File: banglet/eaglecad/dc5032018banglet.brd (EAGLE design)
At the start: 39.8 x 22.6 mm, 43 parts, among them Q3 DMG3415U-7, U2 AP2112(3.3V), U3 MCP73831T-2ACI/OT, U4 CP2104, X1 32.768, X2 JSTPH, X4 20329

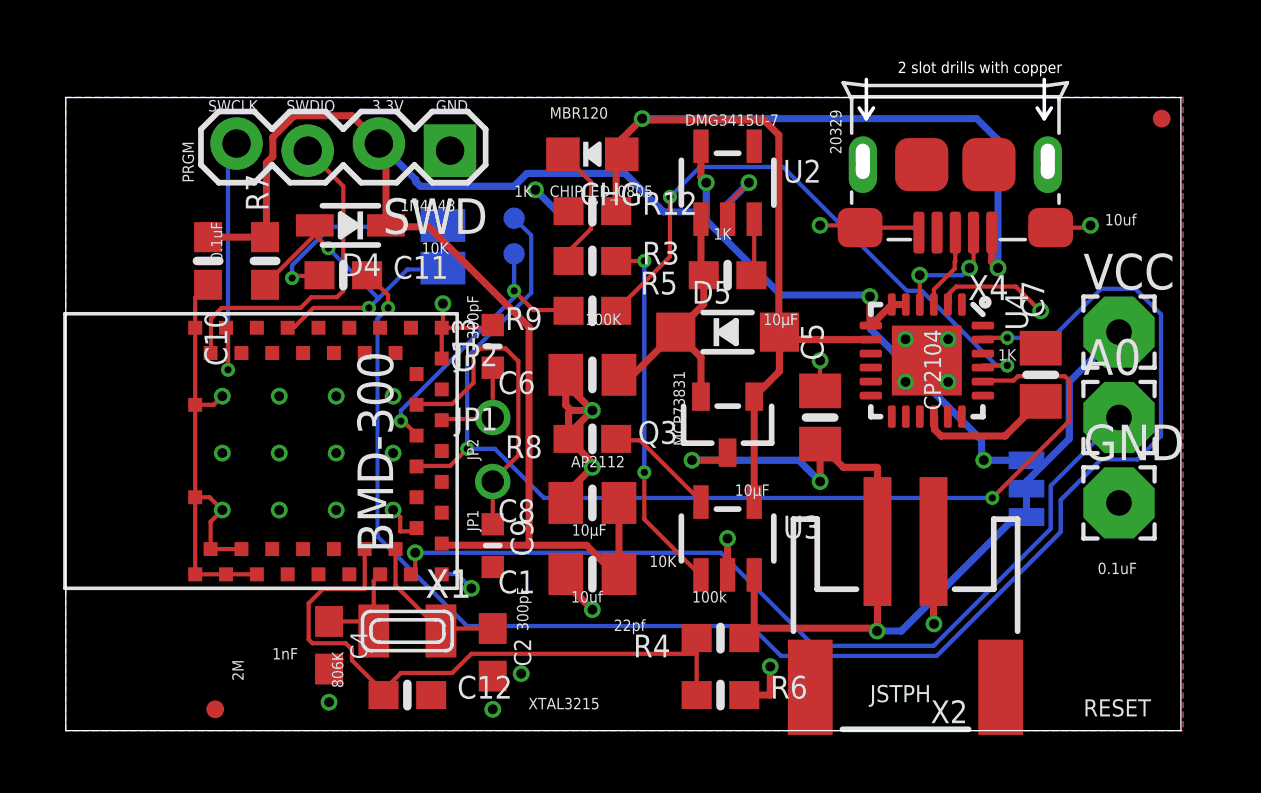
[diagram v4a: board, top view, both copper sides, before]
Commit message: removed NFC parts; deleted stray silk
silk still a mess.  I *think* I got all the stray labels.
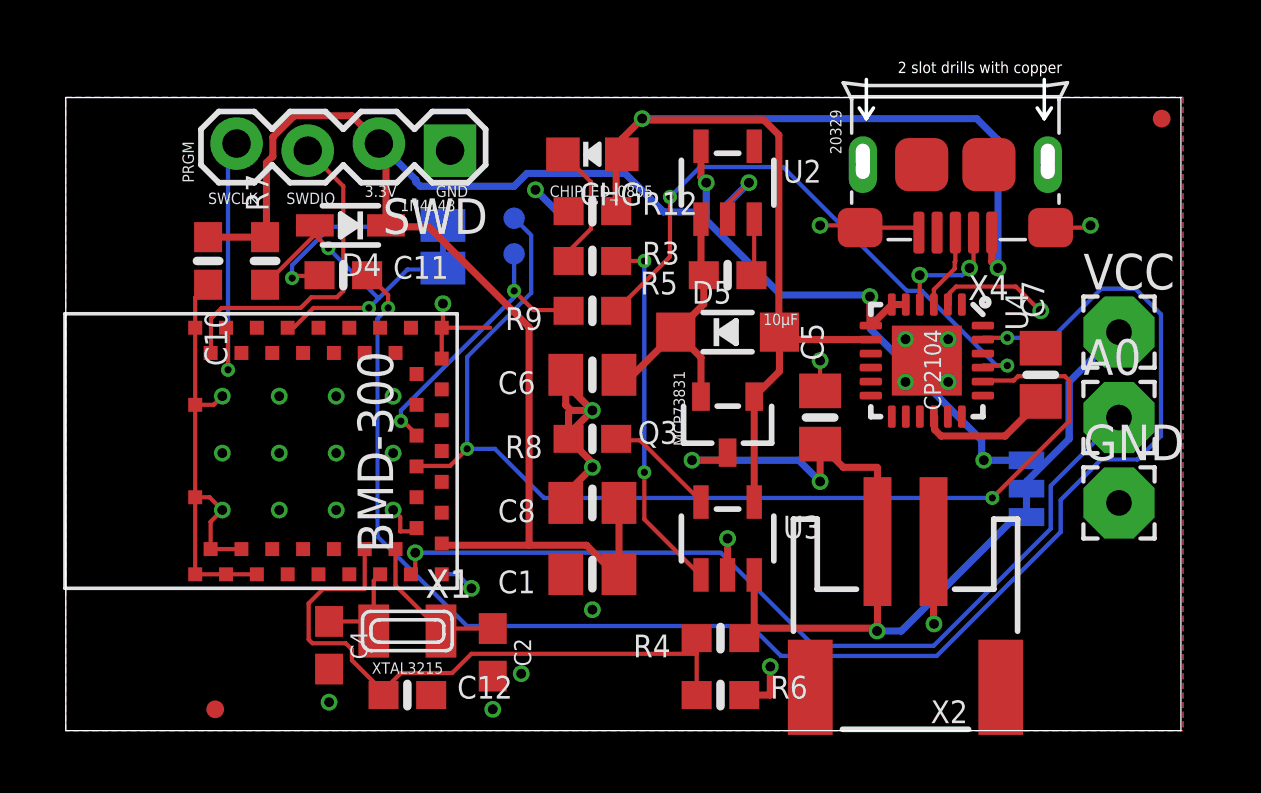
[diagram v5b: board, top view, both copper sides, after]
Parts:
- removed C13, C9: 300pF, microbuilder:_0603MP
- removed JP1, JP2: (no value), microbuilder:1X01_2MM
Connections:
- removed net N$6: C9.1, JP1.1, U1.P26
- removed net P0.09/NFC1: C13.1, JP2.1, U1.P25
- net GND: no longer C13.2, C9.2
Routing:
- net N$6: track 11.4 -> 0.00 mm
- net P0.09/NFC1: track 3.66 -> 0.00 mm
- net GND: track 56.4 -> 54.9 mm
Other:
- board text removed: "0.1uF"
- board text removed: "100K"
- board text removed: "100k"
- board text removed: "10K"
- board text removed: "10uf"
- board text removed: "1K"
- board text removed: "1nF"
- board text removed: "22pf"
- board text removed: "2M"
- board text removed: "300pF"
- board text removed: "806K"
- board text removed: "A0"
- board text removed: "AP2112"
- board text removed: "DMG3415U-7"
- board text removed: "JP1"
- board text removed: "JP2"
- board text removed: "JSTPH"
- board text removed: "MBR120"
- board text removed: "RESET"
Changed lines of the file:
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@@
 <text x="11.684" y="37.592" size="1.27" layer="21" rot="R90">BMD-300</text>
 <text x="31.242" y="42.672" size="0.6096" layer="21" rot="R90">CP2104</text>
-<text x="10.922" y="53.34" size="0.4064" layer="21">3.3V</text>
-<text x="13.208" y="53.34" size="0.4064" layer="21">GND</text>
-<text x="7.874" y="53.34" size="0.4064" layer="21">SWDIO</text>
-<text x="5.08" y="53.34" size="0.4064" layer="21">SWCLK</text>
+<text x="10.668" y="50.292" size="0.4064" layer="21">3.3V</text>
+<text x="13.208" y="50.292" size="0.4064" layer="21">GND</text>
+<text x="7.874" y="50.038" size="0.4064" layer="21">SWDIO</text>
+<text x="5.08" y="50.038" size="0.4064" layer="21">SWCLK</text>
 <text x="4.572" y="50.8" size="0.4064" layer="21" rot="R90">PRGM</text>
-<text x="17.272" y="53.086" size="0.4064" layer="21">MBR120</text>
-<text x="22.098" y="52.832" size="0.4064" layer="21">DMG3415U-7</text>
 <text x="27.686" y="51.816" size="0.4064" layer="21" rot="R90">20329</text>
-<text x="37.084" y="49.276" size="0.4064" layer="21">10uf</text>
-<text x="5.588" y="48.006" size="0.4064" layer="21" rot="R90">0.1uF</text>
-<text x="12.7" y="48.26" size="0.4064" layer="21">10K</text>
-<text x="23.114" y="48.768" size="0.4064" layer="21">1K</text>
 <text x="24.892" y="45.72" size="0.4064" layer="21">10µF</text>
-<text x="33.274" y="44.45" size="0.4064" layer="21">1K</text>
 <text x="22.098" y="41.402" size="0.4064" layer="21" rot="R90">MCP73831</text>
-<text x="18.034" y="40.64" size="0.4064" layer="21">AP2112</text>
-<text x="18.542" y="45.72" size="0.4064" layer="21">100K</text>
 <text x="11.938" y="49.784" size="0.4064" layer="21">1N4148</text>
-<text x="16.002" y="50.292" size="0.4064" layer="21">1K</text>
 <text x="17.272" y="50.292" size="0.4064" layer="21">CHIPLED_0805</text>
-<text x="14.732" y="45.212" size="0.4064" layer="21" rot="R90">300pF</text>
-<text x="19.304" y="38.608" size="0.4064" layer="21" rot="R180">10µF</text>
-<text x="18.034" y="35.814" size="0.4064" layer="21">10uf</text>
-<text x="23.876" y="39.624" size="0.4064" layer="21">10µF</text>
-<text x="20.828" y="37.084" size="0.4064" layer="21">10K</text>
-<text x="16.51" y="34.798" size="0.4064" layer="21" rot="R90">300pF</text>
-<text x="22.352" y="35.814" size="0.4064" layer="21">100k</text>
-<text x="19.558" y="34.798" size="0.4064" layer="21">22pf</text>
-<text x="16.51" y="32.004" size="0.4064" layer="21">XTAL3215</text>
-<text x="9.906" y="32.766" size="0.4064" layer="21" rot="R90">806K</text>
-<text x="7.366" y="33.782" size="0.4064" layer="21">1nF</text>
-<text x="6.35" y="33.02" size="0.4064" layer="21" rot="R90">2M</text>
-<text x="28.702" y="32.258" size="0.6096" layer="21">JSTPH</text>
-<text x="36.83" y="36.83" size="0.4064" layer="21">0.1uF</text>
-<text x="36.322" y="31.75" size="0.6096" layer="21">RESET</text>
-<text x="14.732" y="40.894" size="0.4064" layer="21" rot="R90">JP2</text>
-<text x="14.732" y="38.354" size="0.4064" layer="21" rot="R90">JP1</text>
-<text x="39.624" y="46.482" size="0.6096" layer="22" rot="MR270">3.3V</text>
-<text x="39.624" y="42.926" size="0.6096" layer="22" rot="MR270">A0</text>
-<text x="39.624" y="40.386" size="0.6096" layer="22" rot="MR270">GND</text>
+<text x="10.922" y="33.274" size="0.4064" layer="21">XTAL3215</text>
 <text x="38.1" y="33.782" size="0.6096" layer="22" rot="MR0">DC503 Banglet
 DefCon26
@@
 <element name="C11" library="microbuilder" package="0603-NO" value="0.1uF" x="9.906" y="47.498"/>
 <element name="C12" library="microbuilder" package="0603-NO" value="1nF" x="12.192" y="32.512"/>
-<element name="C13" library="microbuilder" package="_0603MP" value="300pF" x="15.24" y="44.958" rot="R90"/>
 <element name="C5" library="microbuilder" package="0805-NO" value="10µF" x="26.924" y="42.418" rot="R90"/>
 <element name="C6" library="microbuilder" package="0805-NO" value="10µF" x="18.796" y="43.942" rot="R180"/>
 <element name="C7" library="microbuilder" package="0805-NO" value="10uf" x="34.798" y="43.942" rot="R90"/>
 <element name="C8" library="microbuilder" package="0805-NO" value="10µF" x="18.796" y="39.37" rot="R180"/>
-<element name="C9" library="microbuilder" package="_0603MP" value="300pF" x="15.24" y="37.846" rot="R270"/>
 <element name="CHG" library="microbuilder" package="CHIPLED_0805_NOOUTLINE" value="ORANGE" x="18.796" y="51.816" rot="R90"/>
 <element name="D4" library="microbuilder" package="SOD-323" value="1N4148" x="10.16" y="49.276" rot="R180"/>
 <element name="D5" library="microbuilder" package="SOD-123" value="MBR120" x="23.622" y="45.466"/>
 <element name="GND" library="wirepad" library_urn="urn:adsk.eagle:library:412" package="2,54/0,9" value="WIREPAD2,54/0,9" x="37.592" y="39.37"/>
-<element name="JP1" library="microbuilder" package="1X01_2MM" value="" x="15.24" y="40.132"/>
-<element name="JP2" library="microbuilder" package="1X01_2MM" value="" x="15.24" y="42.418"/>
 <element name="Q3" library="microbuilder" package="SOT23-R" value="DMG3415U-7" x="23.622" y="42.164" rot="R180"/>
 <element name="R12" library="microbuilder" package="0603-NO" value="100k" x="18.796" y="49.784"/>
@@
 <contactref element="U1" pad="P18"/>
 <contactref element="C1" pad="2"/>
-<contactref element="C13" pad="2"/>
-<contactref element="C9" pad="2"/>
 <contactref element="U1" pad="P47"/>
 <contactref element="U1" pad="P1"/>
@@
 <wire x1="26.924" y1="43.368" x2="26.924" y2="44.45" width="0.1524" layer="1"/>
 <via x="26.924" y="44.45" extent="1-16" drill="0.35"/>
-<wire x1="15.24" y1="45.72" x2="15.142" y2="45.622" width="0.1524" layer="1"/>
 <wire x1="15.142" y1="45.622" x2="13.42" y2="45.622" width="0.1524" layer="1"/>
 <wire x1="4.62" y1="45.622" x2="4.62" y2="46.696" width="0.1524" layer="1"/>
 <wire x1="4.62" y1="46.696" x2="5.08" y2="47.156" width="0.1524" layer="1"/>
 <wire x1="17.846" y1="36.83" x2="17.846" y2="36.51" width="0.254" layer="1"/>
-<wire x1="17.846" y1="36.51" x2="18.796" y2="35.56" width="0.254" layer="1"/>
 <wire x1="17.846" y1="39.37" x2="17.846" y2="39.69" width="0.254" layer="1"/>
 <wire x1="17.846" y1="39.69" x2="18.796" y2="40.64" width="0.254" layer="1"/>
@@
 <wire x1="10.65" y1="35.14" x2="9.398" y2="35.14" width="0.1524" layer="1"/>
 </signal>
-<signal name="P0.09/NFC1">
-<contactref element="JP2" pad="1"/>
-<contactref element="C13" pad="1"/>
-<contactref element="U1" pad="P25"/>
-<wire x1="15.24" y1="42.3672" x2="13.4874" y2="42.3672" width="0.1524" layer="1"/>
-<wire x1="13.4874" y1="42.3672" x2="13.42" y2="42.322" width="0.1524" layer="1"/>
-<wire x1="15.24" y1="42.3672" x2="15.24" y2="42.418" width="0.1524" layer="1"/>
-<wire x1="15.24" y1="42.418" x2="15.24" y2="44.196" width="0.1524" layer="1"/>
-</signal>
 <signal name="DIO/P0.13">
 <contactref element="U1" pad="P31"/>
@@
 <contactref element="U1" pad="P38"/>
 </signal>
-<signal name="N$6">
-<contactref element="U1" pad="P26"/>
-<contactref element="JP1" pad="1"/>
-<contactref element="C9" pad="1"/>
-<wire x1="13.7922" y1="42.9006" x2="12.573" y2="42.9006" width="0.1524" layer="1"/>
-<wire x1="14.5542" y1="43.6626" x2="13.7922" y2="42.9006" width="0.1524" layer="1"/>
-<wire x1="14.5542" y1="44.6532" x2="14.5542" y2="43.6626" width="0.1524" layer="1"/>
-<wire x1="14.7828" y1="44.8818" x2="14.5542" y2="44.6532" width="0.1524" layer="1"/>
-<wire x1="15.6972" y1="44.8818" x2="14.7828" y2="44.8818" width="0.1524" layer="1"/>
-<wire x1="16.1544" y1="44.4246" x2="15.6972" y2="44.8818" width="0.1524" layer="1"/>
-<wire x1="16.1544" y1="41.0718" x2="16.1544" y2="44.4246" width="0.1524" layer="1"/>
-<wire x1="15.24" y1="40.1574" x2="16.1544" y2="41.0718" width="0.1524" layer="1"/>
-<wire x1="12.573" y1="42.9006" x2="12.52" y2="42.872" width="0.1524" layer="1"/>
-<wire x1="15.24" y1="40.1574" x2="15.24" y2="40.132" width="0.1524" layer="1"/>
-<wire x1="15.24" y1="40.132" x2="15.24" y2="38.608" width="0.1524" layer="1"/>
-</signal>
 <signal name="N$7">

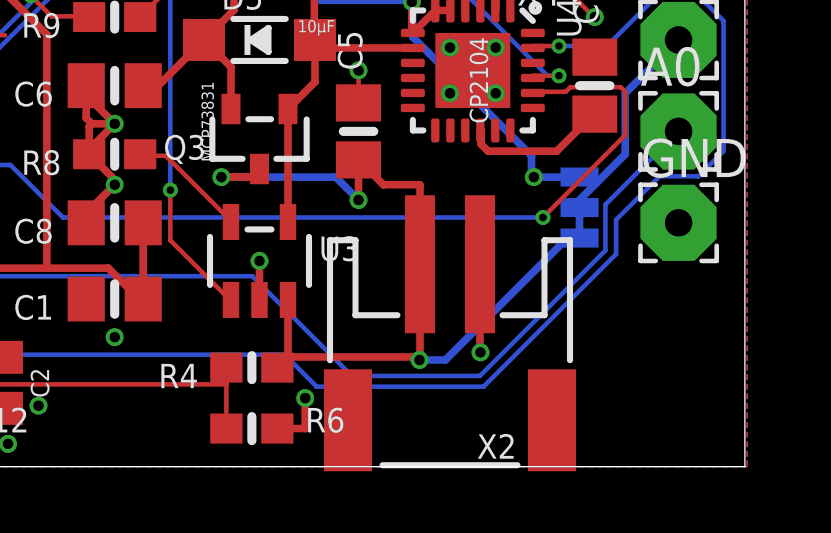
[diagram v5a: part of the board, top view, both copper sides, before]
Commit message: move X2; extend planes to dimension
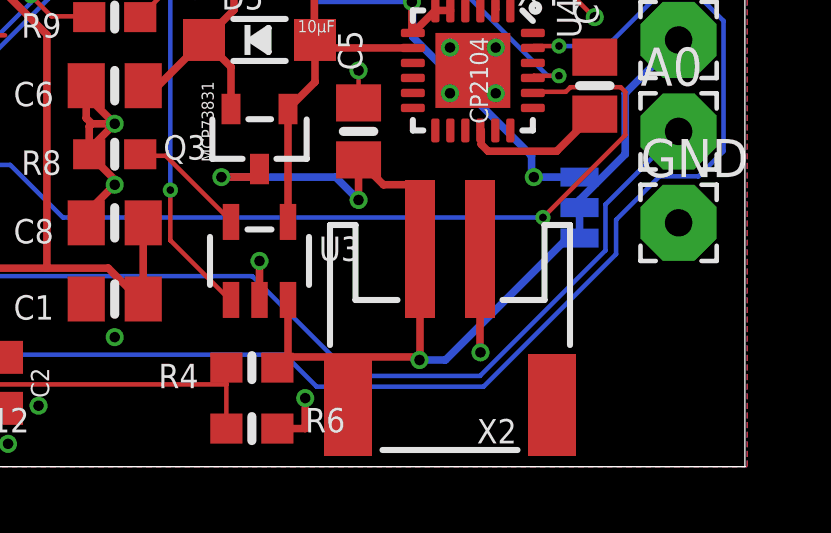
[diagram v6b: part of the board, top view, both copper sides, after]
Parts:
- moved X2 0.51 mm to (30.0, 34.8)
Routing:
- net GND: track 54.9 -> 55.4 mm
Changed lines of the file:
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@@
 <param name="mdViaViaSameLayer" value="8mil"/>
 <param name="mnLayersViaInSmd" value="2"/>
-<param name="mdCopperDimension" value="15mil"/>
+<param name="mdCopperDimension" value="0mil"/>
 <param name="mdDrill" value="6mil"/>
 <param name="mdSmdStop" value="0mil"/>
@@
 <element name="VCC" library="wirepad" library_urn="urn:adsk.eagle:library:412" package="2,54/0,9" value="WIREPAD2,54/0,9" x="37.592" y="45.466"/>
 <element name="X1" library="adafruit2" package="XTAL3215" value="32.768" x="12.192" y="34.798" rot="R180"/>
-<element name="X2" library="microbuilder" package="JSTPH2" value="JSTPH" x="29.972" y="34.29" rot="R180"/>
+<element name="X2" library="microbuilder" package="JSTPH2" value="JSTPH" x="29.972" y="34.798" rot="R180"/>
 <element name="X4" library="microbuilder" package="MICRO-USB5+6P-SMD-0.65-B" value="20329" x="31.75" y="48.768" rot="R180"/>
 <element name="JP3" library="SparkFun-Jumpers" library_urn="urn:adsk.eagle:library:528" package="SMT-JUMPER_3_1-NC_TRACE_SILK" package3d_urn="urn:adsk.eagle:package:39288/1" value="JUMPER-SMT_3_1-NC_TRACE_SILK" x="34.29" y="39.878" rot="MR270"/>
@@
 <wire x1="5.28" y1="42.872" x2="5.588" y2="43.18" width="0.1524" layer="1"/>
 <via x="16.764" y="50.546" extent="1-16" drill="0.35"/>
-<wire x1="30.972" y1="37.99" x2="30.972" y2="35.068" width="0.254" layer="1"/>
+<wire x1="30.972" y1="38.498" x2="30.972" y2="35.068" width="0.254" layer="1"/>
 <wire x1="30.972" y1="35.068" x2="30.988" y2="35.052" width="0.254" layer="1"/>
 <wire x1="24.384" y1="50.8" x2="23.622" y2="50.038" width="0.254" layer="16"/>
@@
 <contactref element="R4" pad="1"/>
 <contactref element="JP3" pad="3"/>
-<wire x1="28.972" y1="37.99" x2="28.972" y2="34.814" width="0.254" layer="1"/>
+<wire x1="28.972" y1="38.498" x2="28.972" y2="34.814" width="0.254" layer="1"/>
 <wire x1="28.972" y1="34.814" x2="28.956" y2="34.798" width="0.254" layer="1"/>
 <via x="28.956" y="34.798" extent="1-16" drill="0.35"/>
@@
 <wire x1="27.752" y1="40.64" x2="28.956" y2="40.64" width="0.254" layer="1"/>
 <wire x1="28.956" y1="40.64" x2="28.972" y2="40.624" width="0.254" layer="1"/>
-<wire x1="28.972" y1="40.624" x2="28.972" y2="37.99" width="0.254" layer="1"/>
+<wire x1="28.972" y1="40.624" x2="28.972" y2="38.498" width="0.254" layer="1"/>
 <wire x1="23.622" y1="41.164" x2="23.352" y2="40.894" width="0.254" layer="1"/>
 <wire x1="23.352" y1="40.894" x2="22.352" y2="40.894" width="0.254" layer="1"/>

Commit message: fix overlap of nc pads with vbat
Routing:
- net VBAT: track 30.2 -> 30.7 mm
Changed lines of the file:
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@@
 <via x="26.924" y="40.132" extent="1-16" drill="0.35"/>
 <wire x1="26.924" y1="40.132" x2="26.924" y2="41.468" width="0.254" layer="1"/>
-<wire x1="24.572" y1="36.7999" x2="24.572" y2="34.898" width="0.254" layer="1"/>
+<wire x1="24.572" y1="36.7999" x2="24.572" y2="35.56" width="0.254" layer="1"/>
+<wire x1="24.572" y1="35.56" x2="24.572" y2="34.898" width="0.254" layer="1"/>
 <wire x1="24.572" y1="34.898" x2="24.218" y2="34.544" width="0.254" layer="1"/>
-<wire x1="28.8798" y1="34.8996" x2="24.6888" y2="34.8996" width="0.254" layer="1"/>
 <wire x1="24.6888" y1="34.8996" x2="24.218" y2="34.544" width="0.254" layer="1"/>
 <wire x1="28.8798" y1="34.8996" x2="28.956" y2="34.798" width="0.254" layer="1"/>
 <wire x1="34.29" y1="38.862" x2="33.8836" y2="38.862" width="0.1524" layer="16"/>
+<wire x1="28.956" y1="34.798" x2="28.194" y2="35.56" width="0.254" layer="1"/>
+<wire x1="28.194" y1="35.56" x2="24.572" y2="35.56" width="0.254" layer="1"/>
 </signal>
 <signal name="EN">
